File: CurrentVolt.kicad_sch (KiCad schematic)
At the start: 6 parts, among them U10 ACS70331EOLCTR-2P5U3

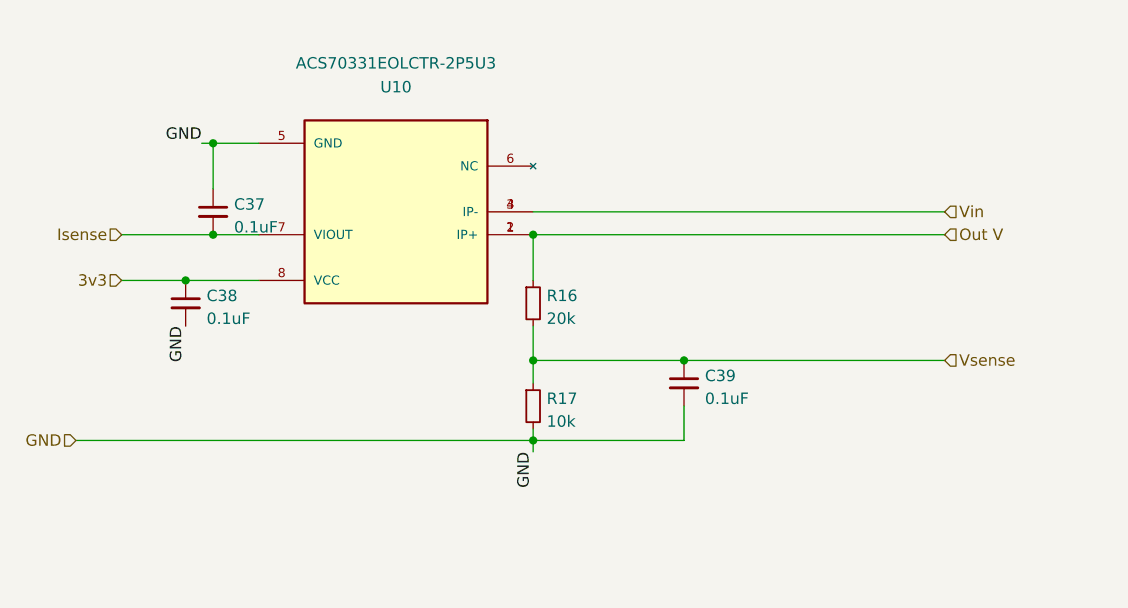
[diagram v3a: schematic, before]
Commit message: new board with SMD
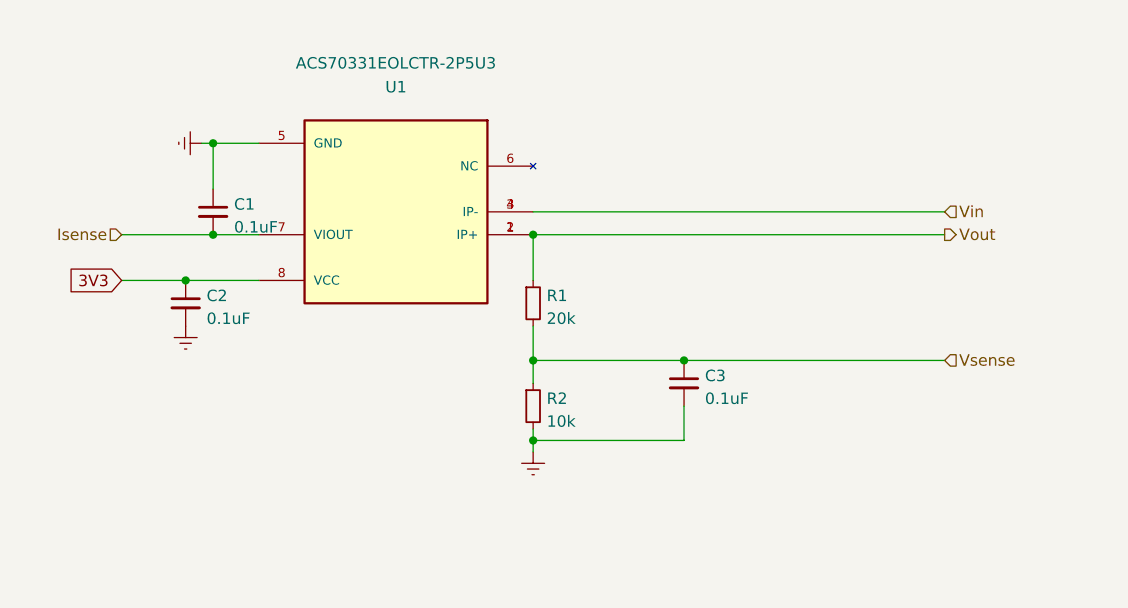
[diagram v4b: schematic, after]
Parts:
- renumbered C37 to C1, C38 to C2, C39 to C3, R16 to R1, R17 to R2, U10 to U1
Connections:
- net 3v3 renamed 3V3
- net GND renamed GNDREF
- net Out V renamed Vout
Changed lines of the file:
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@@
-    (stroke (width 0) (type default) (color 0 0 0 0))
-  )
-  (wire (pts (xy 66.04 114.3) (xy 116.84 114.3))
     (stroke (width 0) (type default) (color 0 0 0 0))
   )
@@
     (stroke (width 0) (type default) (color 0 0 0 0))
   )
-  (label "GND" (at 116.84 115.57 270)
-    (effects (font (size 1.27 1.27)) (justify right bottom))
-  )
-  (label "GND" (at 78.232 101.6 270)
-    (effects (font (size 1.27 1.27)) (justify right bottom))
-  )
-  (label "GND" (at 80.01 81.28 180)
-    (effects (font (size 1.27 1.27)) (justify right bottom))
-  )
-  (hierarchical_label "3v3" (shape input) (at 71.12 96.52 180)
+  (global_label "3V3" (shape input) (at 71.12 96.52 180) (fields_autoplaced)
     (effects (font (size 1.27 1.27)) (justify right))
-  )
-  (hierarchical_label "GND" (shape input) (at 66.04 114.3 180)
-    (effects (font (size 1.27 1.27)) (justify right))
+    (property "Intersheet References" "${INTERSHEET_REFS}" (id 0) (at 65.2882 96.4406 0)
+      (effects (font (size 1.27 1.27)) (justify right))
+    )
   )
   (hierarchical_label "Vin" (shape input) (at 162.56 88.9 0)
@@
     (effects (font (size 1.27 1.27)) (justify right))
   )
-  (hierarchical_label "Out V" (shape input) (at 162.56 91.44 0)
+  (hierarchical_label "Vout" (shape output) (at 162.56 91.44 0)
     (effects (font (size 1.27 1.27)) (justify left))
   )
+  (symbol (lib_id "power:GNDREF") (at 116.84 115.57 0) (unit 1)
+    (in_bom yes) (on_board yes) (fields_autoplaced)
+    (property "Reference" "#PWR03" (id 0) (at 116.84 121.92 0)
+      (effects (font (size 1.27 1.27)) hide)
+    )
+    (property "Value" "GNDREF" (id 1) (at 116.84 120.0134 0)
+      (effects (font (size 1.27 1.27)) hide)
+    )
+    (property "Footprint" "" (id 2) (at 116.84 115.57 0)
+      (effects (font (size 1.27 1.27)) hide)
+    )
+    (property "Datasheet" "" (id 3) (at 116.84 115.57 0)
+      (effects (font (size 1.27 1.27)) hide)
+    )
+    (pin "1")
+  )
   (symbol (lib_id "Device:R_Small") (at 116.84 99.06 0) (unit 1)
     (in_bom yes) (on_board yes) (fields_autoplaced)
-    (property "Reference" "R16" (id 0) (at 118.3386 98.2253 0)
+    (property "Reference" "R1" (id 0) (at 118.3386 98.2253 0)
       (effects (font (size 1.27 1.27)) (justify left))
     )
@@
   (symbol (lib_id "Device:C_Small") (at 78.232 99.06 0) (unit 1)
     (in_bom yes) (on_board yes) (fields_autoplaced)
-    (property "Reference" "C38" (id 0) (at 80.5561 98.2316 0)
+    (property "Reference" "C2" (id 0) (at 80.5561 98.2316 0)
       (effects (font (size 1.27 1.27)) (justify left))
     )
@@
     (pin "1")
     (pin "2")
+  )
+  (symbol (lib_id "power:GNDREF") (at 80.01 81.28 270) (unit 1)
+    (in_bom yes) (on_board yes) (fields_autoplaced)
+    (property "Reference" "#PWR01" (id 0) (at 73.66 81.28 0)
+      (effects (font (size 1.27 1.27)) hide)
+    )
+    (property "Value" "GNDREF" (id 1) (at 75.5666 81.28 0)
+      (effects (font (size 1.27 1.27)) hide)
+    )
+    (property "Footprint" "" (id 2) (at 80.01 81.28 0)
+      (effects (font (size 1.27 1.27)) hide)
+    )
+    (property "Datasheet" "" (id 3) (at 80.01 81.28 0)
+      (effects (font (size 1.27 1.27)) hide)
+    )
+    (pin "1")
   )
   (symbol (lib_id "ACS70331EOLCTR-2P5U3:ACS70331EOLCTR-2P5U3") (at 101.6 88.9 180) (unit 1)
     (in_bom yes) (on_board yes)
-    (property "Reference" "U10" (id 0) (at 101.6 75.0402 0))
+    (property "Reference" "U1" (id 0) (at 101.6 75.0402 0))
     (property "Value" "ACS70331EOLCTR-2P5U3" (id 1) (at 101.6 72.39 0))
     (property "Footprint" "ACS70331EOLCTR-2P5U3:SOIC127P600X175-8N" (id 2) (at 101.6 88.9 0)
@@
   (symbol (lib_id "Device:C_Small") (at 81.28 88.9 0) (unit 1)
     (in_bom yes) (on_board yes) (fields_autoplaced)
-    (property "Reference" "C37" (id 0) (at 83.6041 88.0716 0)
+    (property "Reference" "C1" (id 0) (at 83.6041 88.0716 0)
       (effects (font (size 1.27 1.27)) (justify left))
     )
@@
   (symbol (lib_id "Device:R_Small") (at 116.84 110.49 0) (unit 1)
     (in_bom yes) (on_board yes) (fields_autoplaced)
-    (property "Reference" "R17" (id 0) (at 118.3386 109.6553 0)
+    (property "Reference" "R2" (id 0) (at 118.3386 109.6553 0)
       (effects (font (size 1.27 1.27)) (justify left))
     )
@@
     (pin "2")
   )
+  (symbol (lib_id "power:GNDREF") (at 78.232 101.6 0) (unit 1)
+    (in_bom yes) (on_board yes) (fields_autoplaced)
+    (property "Reference" "#PWR02" (id 0) (at 78.232 107.95 0)
+      (effects (font (size 1.27 1.27)) hide)
+    )
+    (property "Value" "GNDREF" (id 1) (at 78.232 106.0434 0)
+      (effects (font (size 1.27 1.27)) hide)
+    )
+    (property "Footprint" "" (id 2) (at 78.232 101.6 0)
+      (effects (font (size 1.27 1.27)) hide)
+    )
+    (property "Datasheet" "" (id 3) (at 78.232 101.6 0)
+      (effects (font (size 1.27 1.27)) hide)
+    )
+    (pin "1")
+  )
   (symbol (lib_id "Device:C_Small") (at 133.604 107.95 0) (unit 1)
     (in_bom yes) (on_board yes) (fields_autoplaced)
-    (property "Reference" "C39" (id 0) (at 135.9281 107.1216 0)
-      (effects (font (size 1.27 1.27)) (justify left))
-    )
+    (property "Reference" "C3" (id 0) (at 135.9281 107.1216 0)
+      (effects (font (size 1.27 1.27)) (justify left))
+    )

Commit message: Updated improved board for all SMD
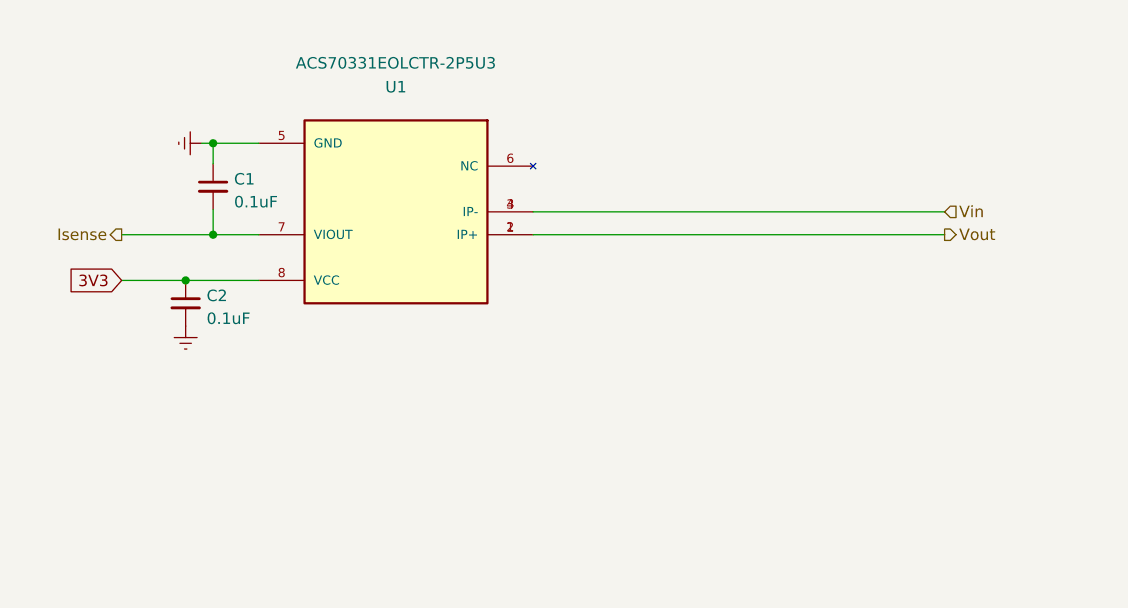
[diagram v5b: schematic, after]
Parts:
- removed C3: 0.1uF, Capacitor_SMD:C_0603_1608Metric, symbol Device:C_Small
- removed R1: 20k, Resistor_SMD:R_0603_1608Metric, symbol Device:R_Small
- removed R2: 10k, Resistor_SMD:R_0603_1608Metric, symbol Device:R_Small
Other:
- moved on the sheet: C1
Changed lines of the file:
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@@
 (kicad_sch (version 20211123) (generator eeschema)
   (paper "A4")
-  (junction (at 133.604 105.41) (diameter 0) (color 0 0 0 0)
-  )
-  (junction (at 116.84 91.44) (diameter 0) (color 0 0 0 0)
-  )
-  (junction (at 116.84 105.41) (diameter 0) (color 0 0 0 0)
-  )
-  (junction (at 116.84 114.3) (diameter 0) (color 0 0 0 0)
-  )
   (junction (at 81.28 81.28) (diameter 0) (color 0 0 0 0)
   )
@@
   )
   (wire (pts (xy 80.01 81.28) (xy 81.28 81.28))
-    (stroke (width 0) (type default) (color 0 0 0 0))
-  )
-  (wire (pts (xy 133.604 114.3) (xy 133.604 110.49))
-    (stroke (width 0) (type default) (color 0 0 0 0))
-  )
-  (wire (pts (xy 116.84 91.44) (xy 116.84 96.52))
     (stroke (width 0) (type default) (color 0 0 0 0))
   )
@@
     (stroke (width 0) (type default) (color 0 0 0 0))
   )
-  (wire (pts (xy 116.84 105.41) (xy 116.84 101.6))
-    (stroke (width 0) (type default) (color 0 0 0 0))
-  )
-  (wire (pts (xy 116.84 105.41) (xy 133.604 105.41))
+  (wire (pts (xy 81.28 88.646) (xy 81.28 91.44))
     (stroke (width 0) (type default) (color 0 0 0 0))
   )
@@
     (stroke (width 0) (type default) (color 0 0 0 0))
   )
-  (wire (pts (xy 116.84 114.3) (xy 133.604 114.3))
-    (stroke (width 0) (type default) (color 0 0 0 0))
-  )
-  (wire (pts (xy 116.84 114.3) (xy 116.84 113.03))
-    (stroke (width 0) (type default) (color 0 0 0 0))
-  )
   (wire (pts (xy 116.84 91.44) (xy 162.56 91.44))
     (stroke (width 0) (type default) (color 0 0 0 0))
   )
-  (wire (pts (xy 133.604 105.41) (xy 162.56 105.41))
-    (stroke (width 0) (type default) (color 0 0 0 0))
-  )
-  (wire (pts (xy 116.84 115.57) (xy 116.84 114.3))
-    (stroke (width 0) (type default) (color 0 0 0 0))
-  )
-  (wire (pts (xy 81.28 81.28) (xy 81.28 86.36))
-    (stroke (width 0) (type default) (color 0 0 0 0))
-  )
-  (wire (pts (xy 116.84 107.95) (xy 116.84 105.41))
+  (wire (pts (xy 81.28 81.28) (xy 81.28 83.566))
     (stroke (width 0) (type default) (color 0 0 0 0))
   )
@@
     (effects (font (size 1.27 1.27)) (justify left))
   )
-  (hierarchical_label "Vsense" (shape input) (at 162.56 105.41 0)
-    (effects (font (size 1.27 1.27)) (justify left))
-  )
-  (hierarchical_label "Isense" (shape input) (at 71.12 91.44 180)
+  (hierarchical_label "Isense" (shape output) (at 71.12 91.44 180)
     (effects (font (size 1.27 1.27)) (justify right))
   )
   (hierarchical_label "Vout" (shape output) (at 162.56 91.44 0)
     (effects (font (size 1.27 1.27)) (justify left))
-  )
-  (symbol (lib_id "power:GNDREF") (at 116.84 115.57 0) (unit 1)
-    (in_bom yes) (on_board yes) (fields_autoplaced)
-    (property "Reference" "#PWR03" (id 0) (at 116.84 121.92 0)
-      (effects (font (size 1.27 1.27)) hide)
-    )
-    (property "Value" "GNDREF" (id 1) (at 116.84 120.0134 0)
-      (effects (font (size 1.27 1.27)) hide)
-    )
-    (property "Footprint" "" (id 2) (at 116.84 115.57 0)
-      (effects (font (size 1.27 1.27)) hide)
-    )
-    (property "Datasheet" "" (id 3) (at 116.84 115.57 0)
-      (effects (font (size 1.27 1.27)) hide)
-    )
-    (pin "1")
-  )
-  (symbol (lib_id "Device:R_Small") (at 116.84 99.06 0) (unit 1)
-    (in_bom yes) (on_board yes) (fields_autoplaced)
-    (property "Reference" "R1" (id 0) (at 118.3386 98.2253 0)
-      (effects (font (size 1.27 1.27)) (justify left))
-    )
-    (property "Value" "20k" (id 1) (at 118.3386 100.7622 0)
-      (effects (font (size 1.27 1.27)) (justify left))
-    )
-    (property "Footprint" "Resistor_SMD:R_0603_1608Metric" (id 2) (at 116.84 99.06 0)
-      (effects (font (size 1.27 1.27)) hide)
-    )
-    (property "Datasheet" "~" (id 3) (at 116.84 99.06 0)
-      (effects (font (size 1.27 1.27)) hide)
-    )
-    (pin "1")
-    (pin "2")
   )
   (symbol (lib_id "Device:C_Small") (at 78.232 99.06 0) (unit 1)
@@
     (pin "8")
   )
-  (symbol (lib_id "Device:C_Small") (at 81.28 88.9 0) (unit 1)
+  (symbol (lib_id "Device:C_Small") (at 81.28 86.106 0) (unit 1)
     (in_bom yes) (on_board yes) (fields_autoplaced)
-    (property "Reference" "C1" (id 0) (at 83.6041 88.0716 0)
+    (property "Reference" "C1" (id 0) (at 83.6041 85.2776 0)
       (effects (font (size 1.27 1.27)) (justify left))
     )
-    (property "Value" "0.1uF" (id 1) (at 83.6041 90.6085 0)
+    (property "Value" "0.1uF" (id 1) (at 83.6041 87.8145 0)
       (effects (font (size 1.27 1.27)) (justify left))
     )
-    (property "Footprint" "Capacitor_SMD:C_0603_1608Metric" (id 2) (at 81.28 88.9 0)
+    (property "Footprint" "Capacitor_SMD:C_0603_1608Metric" (id 2) (at 81.28 86.106 0)
       (effects (font (size 1.27 1.27)) hide)
     )
-    (property "Datasheet" "~" (id 3) (at 81.28 88.9 0)
-      (effects (font (size 1.27 1.27)) hide)
-    )
-    (pin "1")
-    (pin "2")
-  )
-  (symbol (lib_id "Device:R_Small") (at 116.84 110.49 0) (unit 1)
-    (in_bom yes) (on_board yes) (fields_autoplaced)
-    (property "Reference" "R2" (id 0) (at 118.3386 109.6553 0)
-      (effects (font (size 1.27 1.27)) (justify left))
-    )
-    (property "Value" "10k" (id 1) (at 118.3386 112.1922 0)
-      (effects (font (size 1.27 1.27)) (justify left))
-    )
-    (property "Footprint" "Resistor_SMD:R_0603_1608Metric" (id 2) (at 116.84 110.49 0)
-      (effects (font (size 1.27 1.27)) hide)
-    )
-    (property "Datasheet" "~" (id 3) (at 116.84 110.49 0)
+    (property "Datasheet" "~" (id 3) (at 81.28 86.106 0)
       (effects (font (size 1.27 1.27)) hide)
     )
@@
     (pin "1")
   )
-  (symbol (lib_id "Device:C_Small") (at 133.604 107.95 0) (unit 1)
-    (in_bom yes) (on_board yes) (fields_autoplaced)
-    (property "Reference" "C3" (id 0) (at 135.9281 107.1216 0)
-      (effects (font (size 1.27 1.27)) (justify left))
-    )
-    (property "Value" "0.1uF" (id 1) (at 135.9281 109.6585 0)
-      (effects (font (size 1.27 1.27)) (justify left))
-    )
-    (property "Footprint" "Capacitor_SMD:C_0603_1608Metric" (id 2) (at 133.604 107.95 0)
-      (effects (font (size 1.27 1.27)) hide)
-    )
-    (property "Datasheet" "~" (id 3) (at 133.604 107.95 0)
-      (effects (font (size 1.27 1.27)) hide)
-    )
-    (pin "1")
-    (pin "2")
-  )
 )

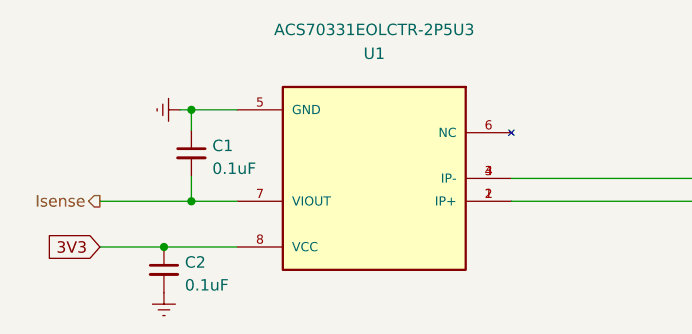
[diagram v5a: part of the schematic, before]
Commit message: repositioned signal wires and started mapping OLED and rotary encoder
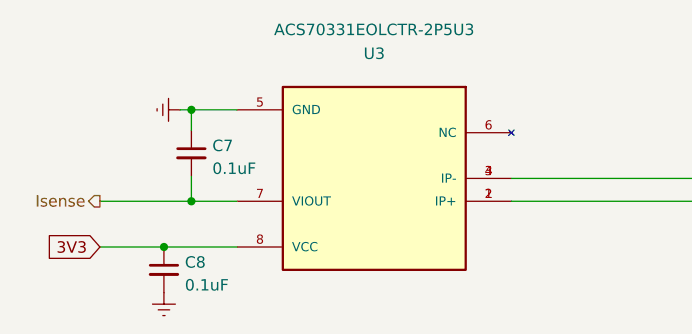
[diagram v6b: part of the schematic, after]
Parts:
- renumbered C1 to C7, C2 to C8, U1 to U3
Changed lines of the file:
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@@
   (symbol (lib_id "Device:C_Small") (at 78.232 99.06 0) (unit 1)
     (in_bom yes) (on_board yes) (fields_autoplaced)
-    (property "Reference" "C2" (id 0) (at 80.5561 98.2316 0)
+    (property "Reference" "C8" (id 0) (at 80.5561 98.2316 0)
       (effects (font (size 1.27 1.27)) (justify left))
     )
@@
   (symbol (lib_id "power:GNDREF") (at 80.01 81.28 270) (unit 1)
     (in_bom yes) (on_board yes) (fields_autoplaced)
-    (property "Reference" "#PWR01" (id 0) (at 73.66 81.28 0)
+    (property "Reference" "#PWR07" (id 0) (at 73.66 81.28 0)
       (effects (font (size 1.27 1.27)) hide)
     )
@@
   (symbol (lib_id "ACS70331EOLCTR-2P5U3:ACS70331EOLCTR-2P5U3") (at 101.6 88.9 180) (unit 1)
     (in_bom yes) (on_board yes)
-    (property "Reference" "U1" (id 0) (at 101.6 75.0402 0))
+    (property "Reference" "U3" (id 0) (at 101.6 75.0402 0))
     (property "Value" "ACS70331EOLCTR-2P5U3" (id 1) (at 101.6 72.39 0))
     (property "Footprint" "ACS70331EOLCTR-2P5U3:SOIC127P600X175-8N" (id 2) (at 101.6 88.9 0)
@@
   (symbol (lib_id "Device:C_Small") (at 81.28 86.106 0) (unit 1)
     (in_bom yes) (on_board yes) (fields_autoplaced)
-    (property "Reference" "C1" (id 0) (at 83.6041 85.2776 0)
+    (property "Reference" "C7" (id 0) (at 83.6041 85.2776 0)
       (effects (font (size 1.27 1.27)) (justify left))
     )
@@
   (symbol (lib_id "power:GNDREF") (at 78.232 101.6 0) (unit 1)
     (in_bom yes) (on_board yes) (fields_autoplaced)
-    (property "Reference" "#PWR02" (id 0) (at 78.232 107.95 0)
+    (property "Reference" "#PWR08" (id 0) (at 78.232 107.95 0)
       (effects (font (size 1.27 1.27)) hide)
     )

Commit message: added new op amps and used automated traces due to complexity
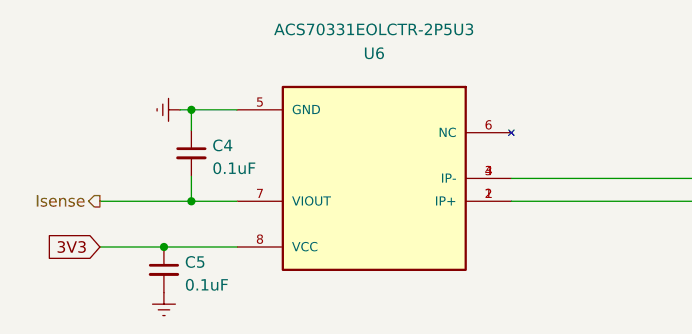
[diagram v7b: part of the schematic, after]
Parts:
- renumbered C7 to C4, C8 to C5, U3 to U6
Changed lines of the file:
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@@
   (symbol (lib_id "Device:C_Small") (at 78.232 99.06 0) (unit 1)
     (in_bom yes) (on_board yes) (fields_autoplaced)
-    (property "Reference" "C8" (id 0) (at 80.5561 98.2316 0)
+    (property "Reference" "C5" (id 0) (at 80.5561 98.2316 0)
       (effects (font (size 1.27 1.27)) (justify left))
     )
@@
   (symbol (lib_id "power:GNDREF") (at 80.01 81.28 270) (unit 1)
     (in_bom yes) (on_board yes) (fields_autoplaced)
-    (property "Reference" "#PWR07" (id 0) (at 73.66 81.28 0)
+    (property "Reference" "#PWR04" (id 0) (at 73.66 81.28 0)
       (effects (font (size 1.27 1.27)) hide)
     )
@@
   (symbol (lib_id "ACS70331EOLCTR-2P5U3:ACS70331EOLCTR-2P5U3") (at 101.6 88.9 180) (unit 1)
     (in_bom yes) (on_board yes)
-    (property "Reference" "U3" (id 0) (at 101.6 75.0402 0))
+    (property "Reference" "U6" (id 0) (at 101.6 75.0402 0))
     (property "Value" "ACS70331EOLCTR-2P5U3" (id 1) (at 101.6 72.39 0))
     (property "Footprint" "ACS70331EOLCTR-2P5U3:SOIC127P600X175-8N" (id 2) (at 101.6 88.9 0)
@@
   (symbol (lib_id "Device:C_Small") (at 81.28 86.106 0) (unit 1)
     (in_bom yes) (on_board yes) (fields_autoplaced)
-    (property "Reference" "C7" (id 0) (at 83.6041 85.2776 0)
+    (property "Reference" "C4" (id 0) (at 83.6041 85.2776 0)
       (effects (font (size 1.27 1.27)) (justify left))
     )
@@
   (symbol (lib_id "power:GNDREF") (at 78.232 101.6 0) (unit 1)
     (in_bom yes) (on_board yes) (fields_autoplaced)
-    (property "Reference" "#PWR08" (id 0) (at 78.232 107.95 0)
+    (property "Reference" "#PWR05" (id 0) (at 78.232 107.95 0)
       (effects (font (size 1.27 1.27)) hide)
     )
